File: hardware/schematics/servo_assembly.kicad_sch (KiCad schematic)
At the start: 3 parts, among them M1 Motor_Servo, Q1 NMOS

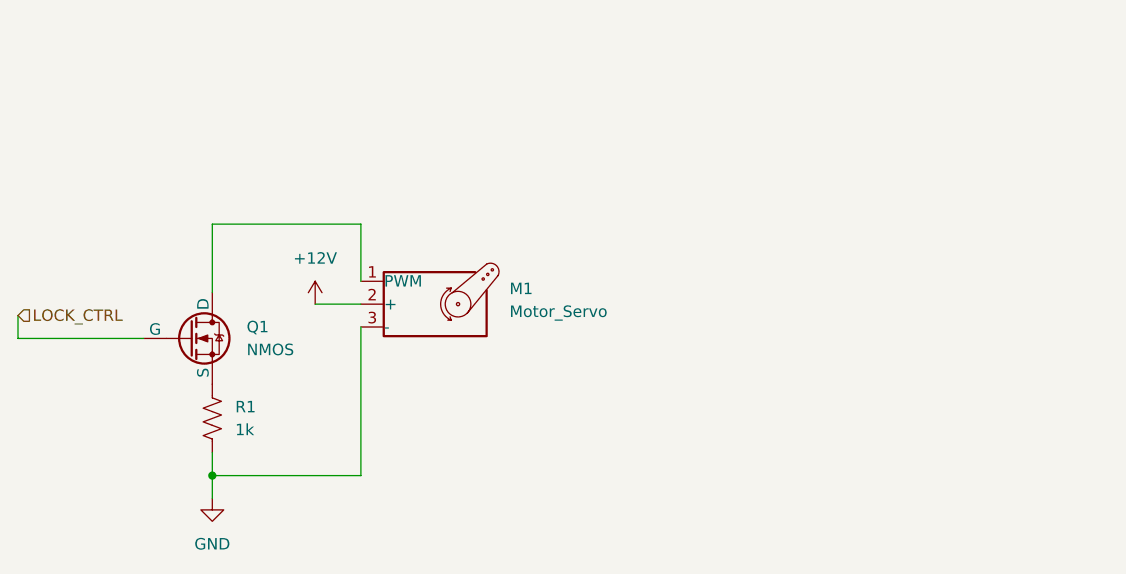
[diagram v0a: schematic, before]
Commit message: added header file (config.h) to esp32 source code to make it look cleaner. Will add more header files in future. Edited schematic - not finished. Switched board from esp32-s3-devkit-c1 to esp32-devkit-v1, since Serial Monitor seems to only work with the second one. Updated .ini file in pio to match
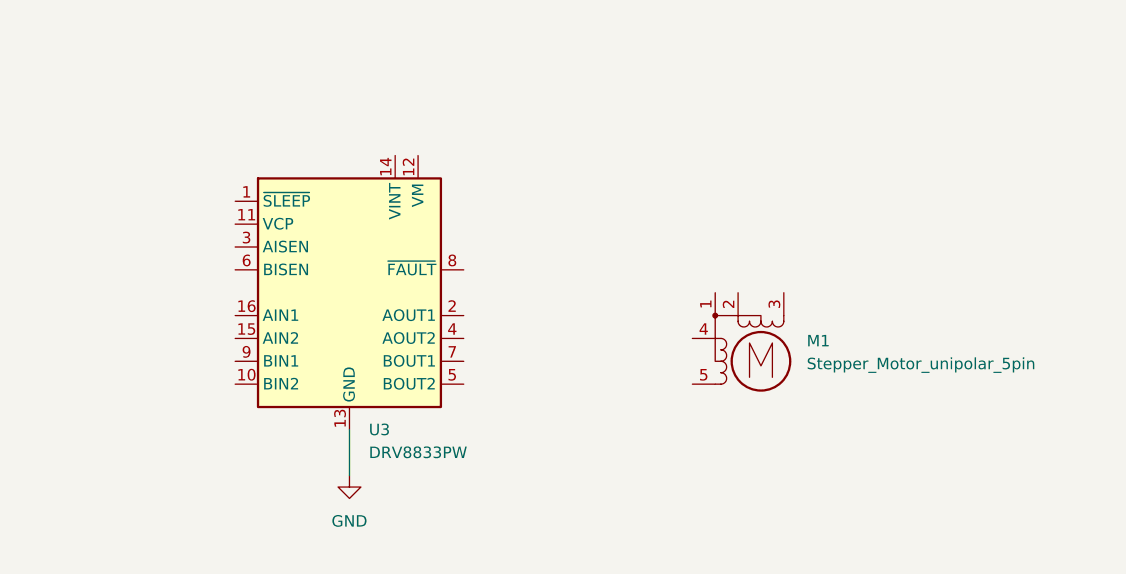
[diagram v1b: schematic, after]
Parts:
- removed M1: Motor_Servo, symbol Motor:Motor_Servo
- removed Q1: NMOS, symbol Simulation_SPICE:NMOS
- removed R1: 1k, symbol Device:R_US
- added M1: Stepper_Motor_unipolar_5pin, symbol Motor:Stepper_Motor_unipolar_5pin
- added U3: DRV8833PW, Package_SO:TSSOP-16_4.4x5mm_P0.65mm, symbol Driver_Motor:DRV8833PW
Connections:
- net GND: now also U3.13 (GND)

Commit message: Modified schematics to reflect design choices. Not finished
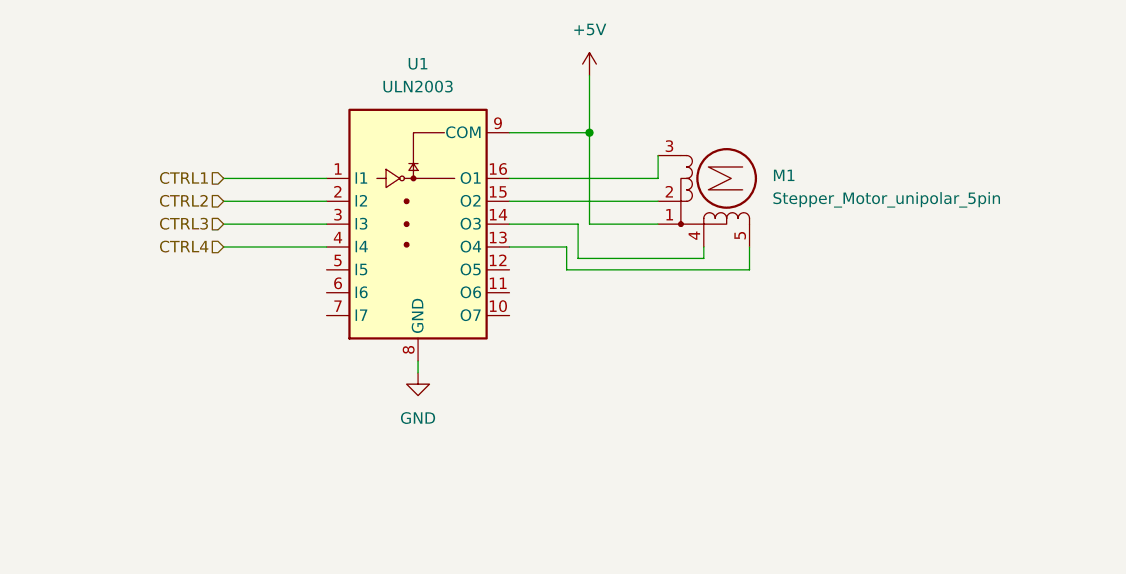
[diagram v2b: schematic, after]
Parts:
- removed U3: DRV8833PW, Package_SO:TSSOP-16_4.4x5mm_P0.65mm, symbol Driver_Motor:DRV8833PW
- added U1: ULN2003, symbol Transistor_Array:ULN2003
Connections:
- net GND: now also U1.8 (GND)
- net +5V: now reaches M1.1
- net +5V: now also U1.9 (COM)
- net at M1.2: now also U1.15 (O2)
- net at M1.3 (-): now also U1.16 (O1)
- net at M1.4: now also U1.14 (O3)
- net at M1.5: now also U1.13 (O4)
- new net CTRL1: U1.1 (I1)
- new net CTRL2: U1.2 (I2)
- new net CTRL3: U1.3 (I3)
- new net CTRL4: U1.4 (I4)
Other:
- moved on the sheet: M1
